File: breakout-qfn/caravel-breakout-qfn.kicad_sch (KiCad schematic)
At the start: 12 parts, among them CON1 REF-182665-01, CON2 REF-182665-01, U1 Caravel_QFN_TT4

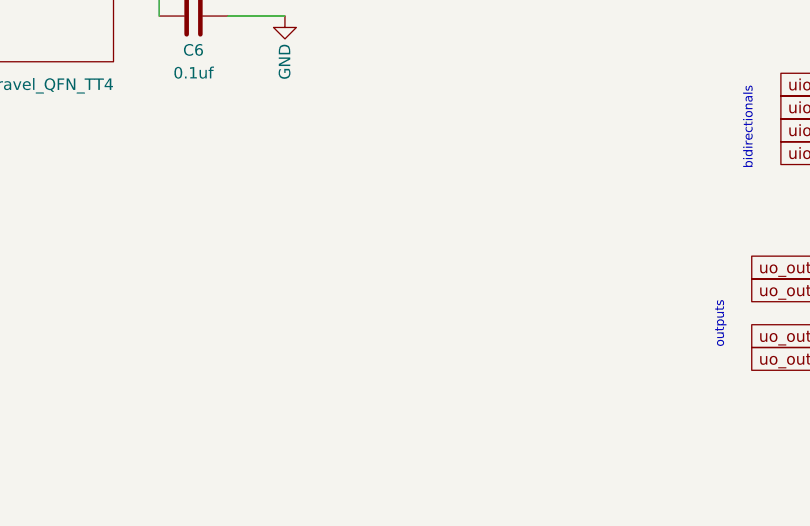
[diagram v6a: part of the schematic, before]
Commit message: Added deglitch/delay on Caravel nRST
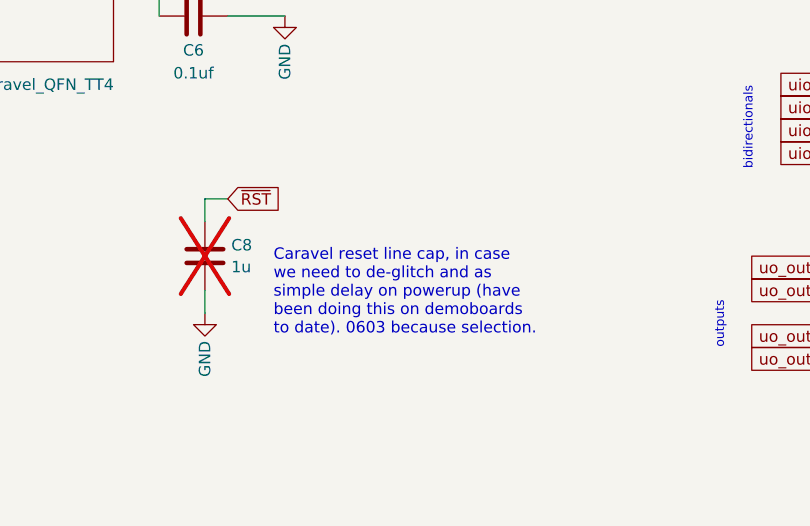
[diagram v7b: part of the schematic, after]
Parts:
- added C8: C_1u_0603_50V, Capacitor_SMD:C_0603_1608Metric, symbol psypassives:C_1u_0603_50V
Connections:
- net GND: now also C8.2
- net ~{RST}: now also C8.1
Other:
- note added: "Caravel reset line cap, in case we need to de-glitch and as simple delay on powerup (have been doing this on demoboards to date). 0603 because selection."
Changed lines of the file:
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@@
+    (stroke (width 0) (type default))
+  )
+  (wire (pts (xy 134.62 147.32) (xy 134.62 149.86))
     (stroke (width 0) (type default))
   )
@@
     (stroke (width 0) (type default))
   )
+  (wire (pts (xy 137.16 137.16) (xy 134.62 137.16))
+    (stroke (width 0) (type default))
+  )
   (wire (pts (xy 45.72 73.66) (xy 45.72 67.31))
     (stroke (width 0) (type default))
@@
     (stroke (width 0) (type default))
   )
+  (wire (pts (xy 134.62 137.16) (xy 134.62 139.7))
+    (stroke (width 0) (type default))
+  )
   (wire (pts (xy 48.26 93.98) (xy 43.18 93.98))
     (stroke (width 0) (type default))
@@
   (wire (pts (xy 213.36 109.22) (xy 218.44 109.22))
     (stroke (width 0) (type default))
+  )
+  (text "Caravel reset line cap, in case \nwe need to de-glitch and as\nsimple delay on powerup (have\nbeen doing this on demoboards\nto date). 0603 because selection."
+    (at 142.24 152.4 0)
+    (effects (font (size 1.27 1.27)) (justify left bottom))
   )
   (text "Caravel QFN Breakout For TinyTapeout" (at 66.04 20.32 0)
@@
     )
   )
+  (global_label "~{RST}" (shape input) (at 137.16 137.16 0) (fields_autoplaced)
+    (effects (font (size 1.27 1.27)) (justify left))
+    (property "Intersheetrefs" "${INTERSHEET_REFS}" (at 1.27 62.23 0)
+      (effects (font (size 1.27 1.27)) hide)
+    )
+  )
   (global_label "ui_in[7]{slash}mio[15]" (shape input) (at 43.18 78.74 180) (fields_autoplaced)
     (effects (font (size 1.27 1.27)) (justify right))
@@
     )
   )
+  (symbol (lib_id "psypassives:C_1u_0603_50V") (at 134.62 143.51 0) (unit 1)
+    (in_bom yes) (on_board yes) (dnp yes) (fields_autoplaced)
+    (property "Reference" "C8" (at 137.541 142.2979 0)
+      (effects (font (size 1.27 1.27)) (justify left))
+    )
+    (property "Value" "C_1u_0603_50V" (at 134.62 146.05 0)
+      (effects (font (size 1.27 1.27)) (justify left) hide)
+    )
+    (property "Footprint" "Capacitor_SMD:C_0603_1608Metric" (at 138.43 142.24 90)
+      (effects (font (size 1.27 1.27)) hide)
+    )
+    (property "Datasheet" "~" (at 134.62 143.51 0)
+      (effects (font (size 1.27 1.27)) hide)
+    )
+    (property "Manufacturer" "GRT188R61H105KE13D" (at 143.51 138.43 90)
+      (effects (font (size 1.27 1.27)) hide)
+    )
+    (property "Vendor" "490-12330-1-ND" (at 140.97 139.7 90)
+      (effects (font (size 1.27 1.27)) hide)
+    )
+    (property "Display Value" "1u" (at 137.541 144.7221 0)
+      (effects (font (size 1.27 1.27)) (justify left))
+    )
+    (pin "1")
+    (pin "2")
+    (instances
+      (project "caravel-breakout-qfn"
+        (path "/b38c65ac-2d57-46f9-9a32-ad09573ee400"
+          (reference "C8") (unit 1)
+        )
+      )
+    )
+  )
   (symbol (lib_id "power:GND") (at 233.68 121.92 90) (unit 1)
     (in_bom yes) (on_board yes) (dnp no)
@@
         )
       )
+    )
+  )
+  (symbol (lib_id "power:GND") (at 134.62 149.86 0) (unit 1)
+    (in_bom yes) (on_board yes) (dnp no)
+    (property "Reference" "#PWR017" (at 134.62 156.21 0)
+      (effects (font (size 1.27 1.27)) hide)
+    )
+    (property "Value" "GND" (at 134.62 154.94 90)
+      (effects (font (size 1.27 1.27)))
+    )
+    (property "Footprint" "" (at 134.62 149.86 0)
+      (effects (font (size 1.27 1.27)) hide)
+    )
+    (property "Datasheet" "" (at 134.62 149.86 0)
+      (effects (font (size 1.27 1.27)) hide)
+    )
+    (pin "1")
+    (instances
+      (project "caravel-breakout-qfn"
+        (path "/b38c65ac-2d57-46f9-9a32-ad09573ee400"
+          (reference "#PWR017") (unit 1)
+        )
+      )

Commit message: TT03p5, as fabbed
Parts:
- C1, C10, C11, C2, C3, C4, C5, C6, C7: MPN (none) -> CL05A104KA5NNNC; MPN_ALT (none) -> GRM155R71E104KE14J
- C8: value C_1u_0603_50V -> 1u
- CON1, CON2: MPN (none) -> FH-00339; MPN_ALT (none) -> REF-182665-01 (or Harwin M20-7812045)
- U1: MPN (none) -> TTASICCHIP03P5
